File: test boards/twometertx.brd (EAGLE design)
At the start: 160 x 100 mm, 12 parts

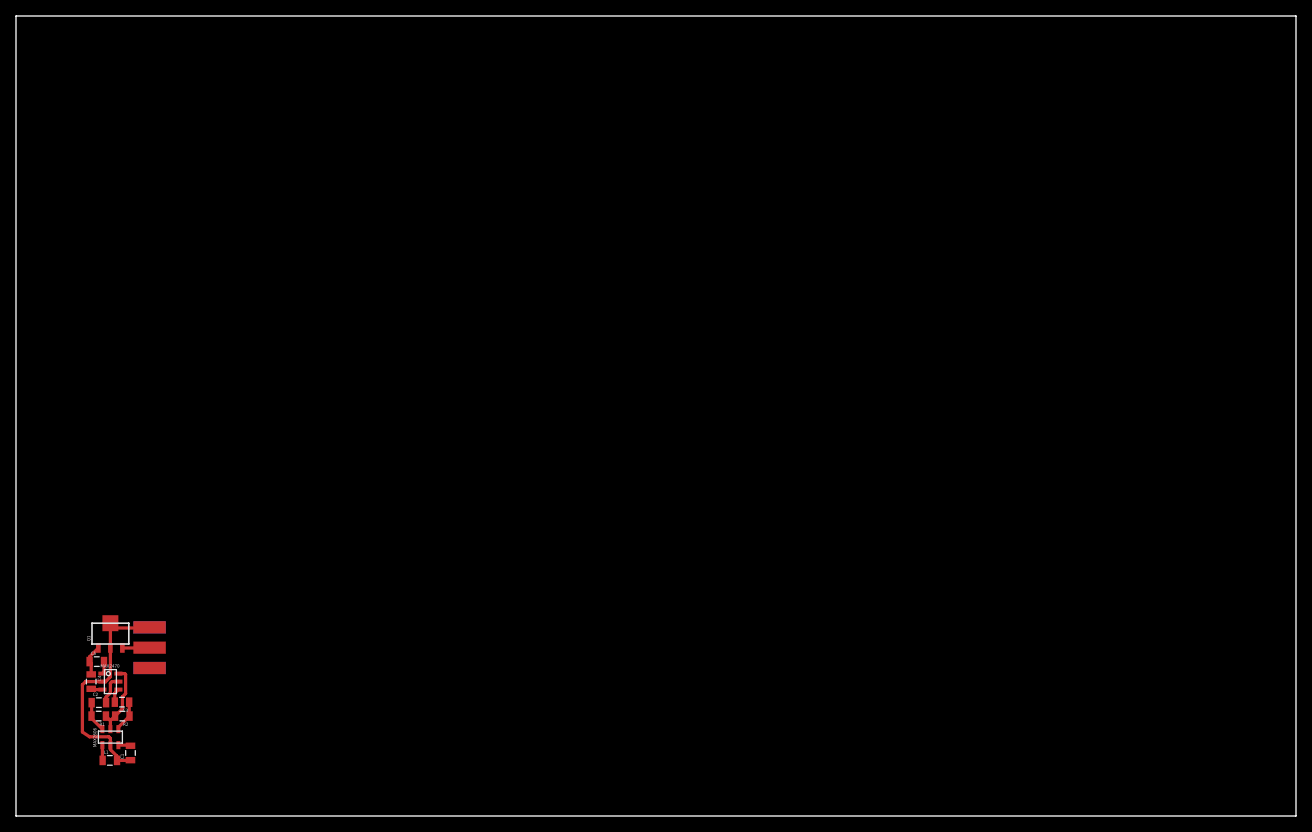
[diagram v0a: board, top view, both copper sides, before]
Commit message: 2 meter rx fixes
added ground pours and 4 pin header to the 2 meter rx for a test board.
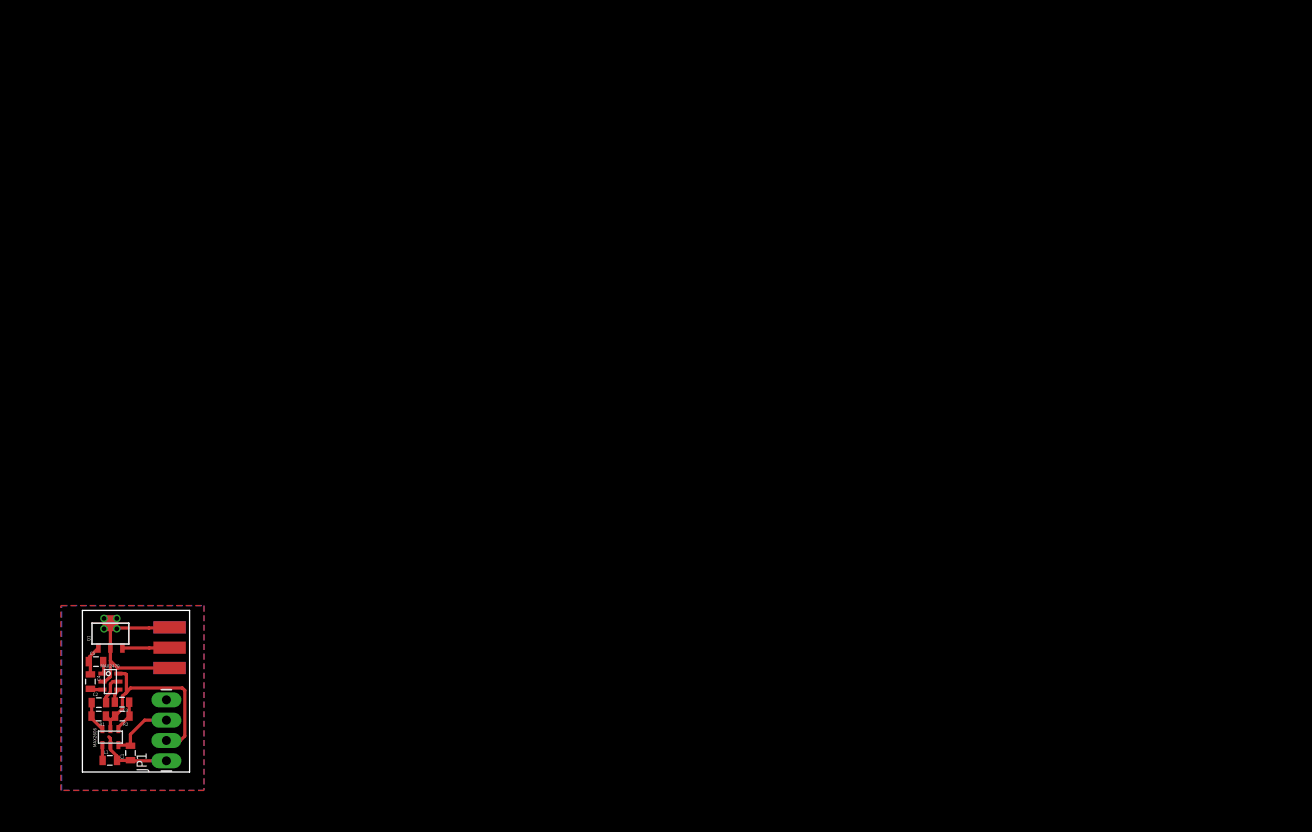
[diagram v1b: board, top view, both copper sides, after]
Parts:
- added JP1: (no value), SparkFun-Connectors:1X04_LONGPADS
- moved J$1 2.50 mm to (19.2, 18.5)
- moved C4 0.10 mm to (9.30, 16.8)
- moved C5 0.10 mm to (10.0, 19.3)
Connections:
- net 5V: now also JP1.2
- net GND: now also JP1.1
- net TUNE: now also JP1.3
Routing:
- net 5V: track 9.38 -> 25.5 mm
- net TUNE: track 1.54 -> 8.20 mm
- net GND: track 29.2 -> 31.9 mm, vias 0 -> 4
- net RFOUT: track 3.42 -> 5.90 mm
- added copper zone on layer 1, net GND
- added copper zone on layer 16, net GND
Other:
- board size 160 x 100 mm -> 13.4 x 20.2 mm

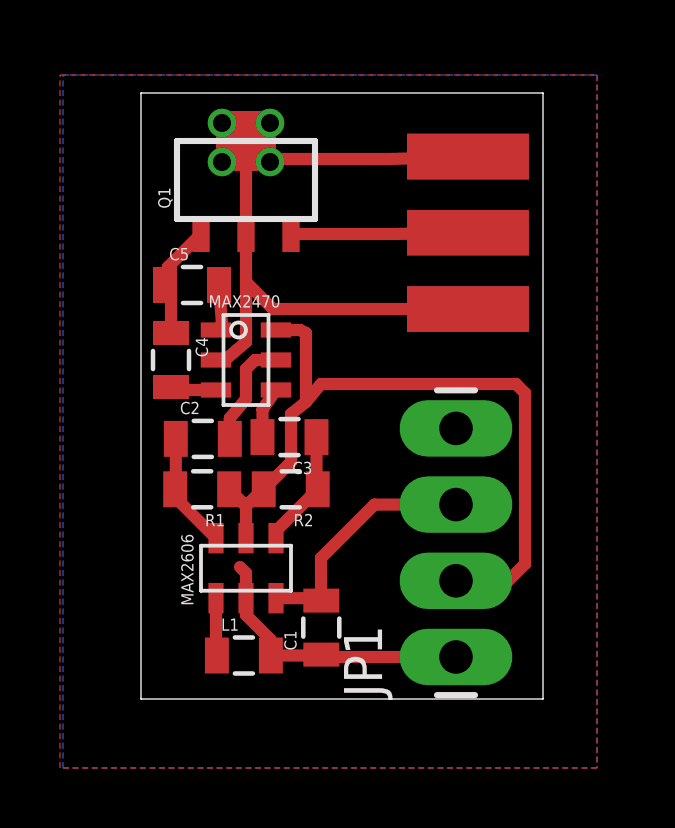
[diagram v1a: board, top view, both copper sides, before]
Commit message: 2 meter tx rf amp bias
added bias circuit to RF amplifier
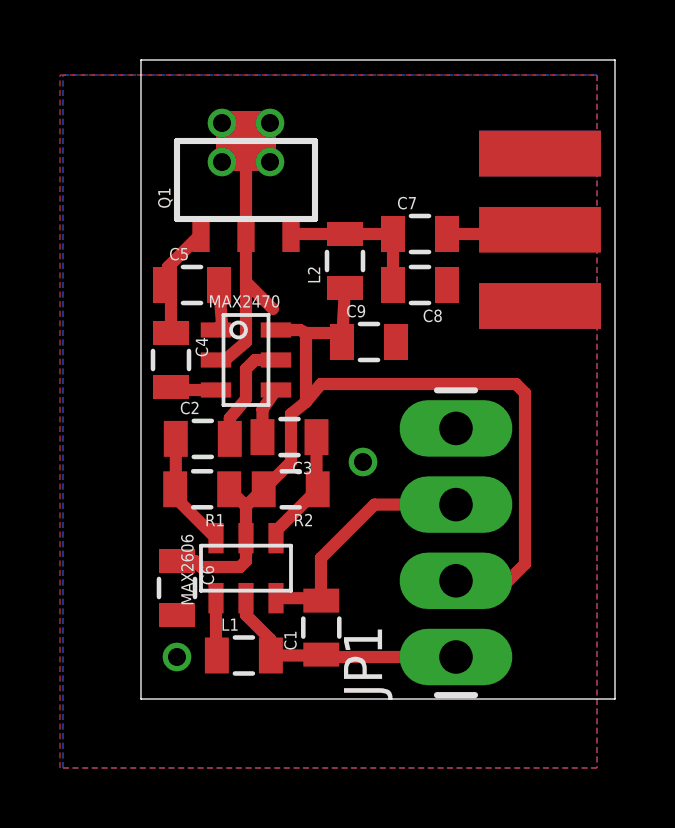
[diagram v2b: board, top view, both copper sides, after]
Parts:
- added C6, C7, C8, C9: (no value), SparkFun-Capacitors:0805
- added L2: (no value), SparkFun-Passives:0805
- moved J$1 2.40 mm to (21.6, 18.6)
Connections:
- new net N$3: C7.1, C8.2, L2.2, Q1.3
- net 5V: now also C6.1, C9.1, L2.1
- net GND: now also C6.2, C8.1, C9.2
- net RFOUT: now also C7.2; no longer Q1.3
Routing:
- net GND: track 31.9 -> 17.2 mm, vias 4 -> 6
- net 5V: track 25.5 -> 31.8 mm
- net N$3: track 0.00 -> 5.10 mm
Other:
- board size 13.4 x 20.2 mm -> 15.8 x 21.3 mm
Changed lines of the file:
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@@
 <board>
 <plain>
-<wire x1="8.3" y1="5.5" x2="21.7" y2="5.5" width="0" layer="20"/>
-<wire x1="21.7" y1="5.5" x2="21.7" y2="25.7" width="0" layer="20"/>
-<wire x1="21.7" y1="25.7" x2="8.3" y2="25.7" width="0" layer="20"/>
-<wire x1="8.3" y1="25.7" x2="8.3" y2="5.5" width="0" layer="20"/>
+<wire x1="8.3" y1="5.5" x2="24.1" y2="5.5" width="0" layer="20"/>
+<wire x1="24.1" y1="5.5" x2="24.1" y2="26.8" width="0" layer="20"/>
+<wire x1="24.1" y1="26.8" x2="8.3" y2="26.8" width="0" layer="20"/>
+<wire x1="8.3" y1="26.8" x2="8.3" y2="5.5" width="0" layer="20"/>
 </plain>
 <attributes>
@@
 <element name="C4" library="SparkFun-Capacitors" package="0805" value="" x="9.3" y="16.8" rot="R270"/>
 <element name="C5" library="SparkFun-Capacitors" package="0805" value="" x="10" y="19.3"/>
-<element name="J$1" library="SparkFun-Connectors" package="SMA-EDGE" value="SMA_EDGE" x="19.2" y="18.5" rot="R90"/>
+<element name="J$1" library="SparkFun-Connectors" package="SMA-EDGE" value="SMA_EDGE" x="21.6" y="18.6" rot="R90"/>
 <element name="Q1" library="SparkFun-DiscreteSemi" package="SOT89" value="" x="11.8" y="22.8"/>
 <element name="JP1" library="SparkFun-Connectors" package="1X04_LONGPADS" value="" x="18.8" y="6.9" rot="R90"/>
+<element name="C6" library="SparkFun-Capacitors" package="0805" value="" x="9.5" y="9.2" rot="R270"/>
+<element name="L2" library="SparkFun-Passives" package="0805" value="" x="15.1" y="20.1" rot="R90"/>
+<element name="C7" library="SparkFun-Capacitors" package="0805" value="" x="17.6" y="21"/>
+<element name="C8" library="SparkFun-Capacitors" package="0805" value="" x="17.6" y="19.3" rot="R180"/>
+<element name="C9" library="SparkFun-Capacitors" package="0805" value="" x="15.9" y="17.4"/>
 </elements>
 <signals>
@@
 <wire x1="12.63" y1="6.95" x2="14.28" y2="6.95" width="0.4064" layer="1"/>
 <wire x1="14.28" y1="6.95" x2="14.31" y2="6.98" width="0.4064" layer="1"/>
-<wire x1="11.8" y1="8.86" x2="11.8" y2="9.7" width="0.4064" layer="1"/>
-<wire x1="11.8" y1="9.7" x2="11.6" y2="9.9" width="0.4064" layer="1"/>
 <wire x1="10.8" y1="16.8" x2="11.1" y2="16.8" width="0.4064" layer="1"/>
 <wire x1="11.1" y1="16.8" x2="11.8" y2="17.4" width="0.4064" layer="1"/>
@@
 <wire x1="11.8" y1="21" x2="11.8" y2="23.2" width="0.4064" layer="1"/>
 <wire x1="11.8" y1="23.2" x2="12.1" y2="23.5" width="0.4064" layer="1"/>
-<wire x1="12.1" y1="23.5" x2="16.62" y2="23.5" width="0.4064" layer="1"/>
-<wire x1="16.62" y1="23.5" x2="19.2" y2="23.58" width="0.4064" layer="1"/>
 <contactref element="JP1" pad="1"/>
 <wire x1="18.8" y1="6.9" x2="14.39" y2="6.9" width="0.4064" layer="1"/>
 <wire x1="14.39" y1="6.9" x2="14.31" y2="6.98" width="0.4064" layer="1"/>
-<wire x1="19.2" y1="18.5" x2="12.7" y2="18.5" width="0.4064" layer="1"/>
 <wire x1="12.7" y1="18.5" x2="11.8" y2="19.4" width="0.4064" layer="1"/>
 <polygon width="0.4064" layer="16">
@@
 <via x="12.6" y="23.4" extent="1-16" drill="0.6" shape="square"/>
 <via x="11" y="23.4" extent="1-16" drill="0.6" shape="square"/>
-<wire x1="19.2" y1="18.5" x2="19.2" y2="18.5" width="0" layer="19" extent="1-16"/>
+<contactref element="C6" pad="2"/>
+<via x="15.7" y="13.4" extent="1-16" drill="0.6"/>
+<via x="9.5" y="6.9" extent="1-16" drill="0.6"/>
+<contactref element="C9" pad="2"/>
+<contactref element="C8" pad="1"/>
 </signal>
 <signal name="TUNE">
@@
 <wire x1="20.8" y1="16" x2="14.3" y2="16" width="0.4064" layer="1"/>
 <wire x1="14.3" y1="16" x2="13.8" y2="15.4" width="0.4064" layer="1"/>
+<contactref element="C6" pad="1"/>
+<wire x1="9.5" y1="10.1" x2="10.1" y2="10.1" width="0.4064" layer="1"/>
+<wire x1="10.1" y1="10.1" x2="10.3" y2="9.9" width="0.4064" layer="1"/>
+<wire x1="10.3" y1="9.9" x2="11.6" y2="9.9" width="0.4064" layer="1"/>
+<wire x1="11.6" y1="9.9" x2="11.8" y2="10.1" width="0.4064" layer="1"/>
+<wire x1="11.8" y1="10.1" x2="11.8" y2="10.86" width="0.4064" layer="1"/>
+<contactref element="L2" pad="1"/>
+<contactref element="C9" pad="1"/>
+<wire x1="13.8" y1="17.7" x2="14.7" y2="17.7" width="0.4064" layer="1"/>
+<wire x1="14.7" y1="17.7" x2="15" y2="17.4" width="0.4064" layer="1"/>
+<wire x1="15" y1="17.4" x2="15.1" y2="19.2" width="0.4064" layer="1"/>
 </signal>
 <signal name="IN+">
@@
 </signal>
 <signal name="RFOUT">
+<contactref element="J$1" pad="SIG"/>
+<contactref element="C7" pad="2"/>
+<wire x1="18.5" y1="21" x2="23.06" y2="21" width="0.4064" layer="1"/>
+<wire x1="23.06" y1="21" x2="21.6" y2="21.14" width="0.4064" layer="1"/>
+</signal>
+<signal name="N$3">
+<contactref element="L2" pad="2"/>
+<contactref element="C7" pad="1"/>
+<contactref element="C8" pad="2"/>
+<contactref element="C8" pad="2"/>
 <contactref element="Q1" pad="3"/>
-<contactref element="J$1" pad="SIG"/>
-<wire x1="13.3" y1="21" x2="16.66" y2="21" width="0.4064" layer="1"/>
-<wire x1="16.66" y1="21" x2="19.2" y2="21.04" width="0.4064" layer="1"/>
+<wire x1="13.3" y1="21" x2="15.1" y2="21" width="0.4064" layer="1"/>
+<wire x1="15.1" y1="21" x2="16.7" y2="21" width="0.4064" layer="1"/>
+<wire x1="16.7" y1="21" x2="16.7" y2="19.3" width="0.4064" layer="1"/>
 </signal>
 </signals>
